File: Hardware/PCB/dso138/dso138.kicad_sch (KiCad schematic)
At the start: 41 parts, among them J1 Synth_power_2x5, J2 Conn_01x02, J3 Conn_01x02, J4 Conn_01x02, J5 Conn_02x04_Odd_Even, J6 Conn_02x04_Odd_Even, J7 Conn_02x04_Odd_Even, J8 Conn_02x04_Odd_Even, J9 Conn_01x02, SW1 SW_Push, SW2 SW_Push, SW3 SW_Push, SW4 SW_Push, SW5 SW_Push, SW6 SW_DP3T, SW7 SW_DP3T, SW8 SW_DP3T, U1 TL072, U2 L78L09_TO92

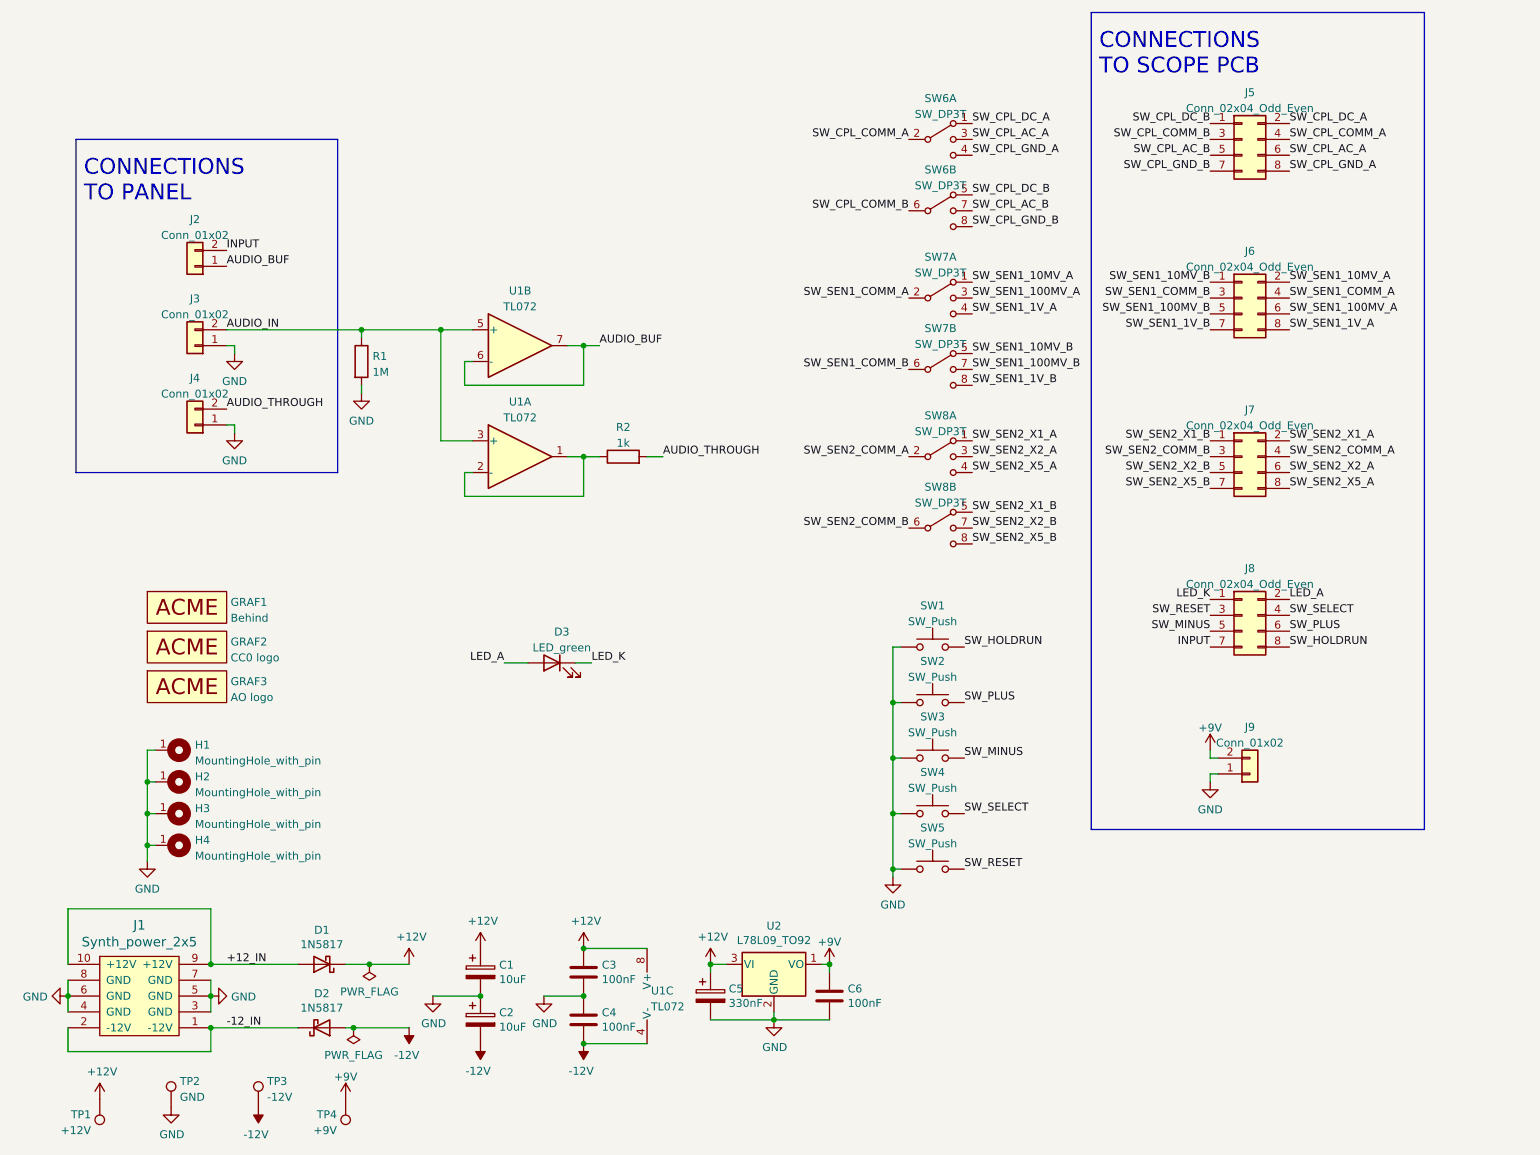
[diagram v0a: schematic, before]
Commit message: KiCad 7; Reorg schematic and add panel components & connectors; re-enable 3D models
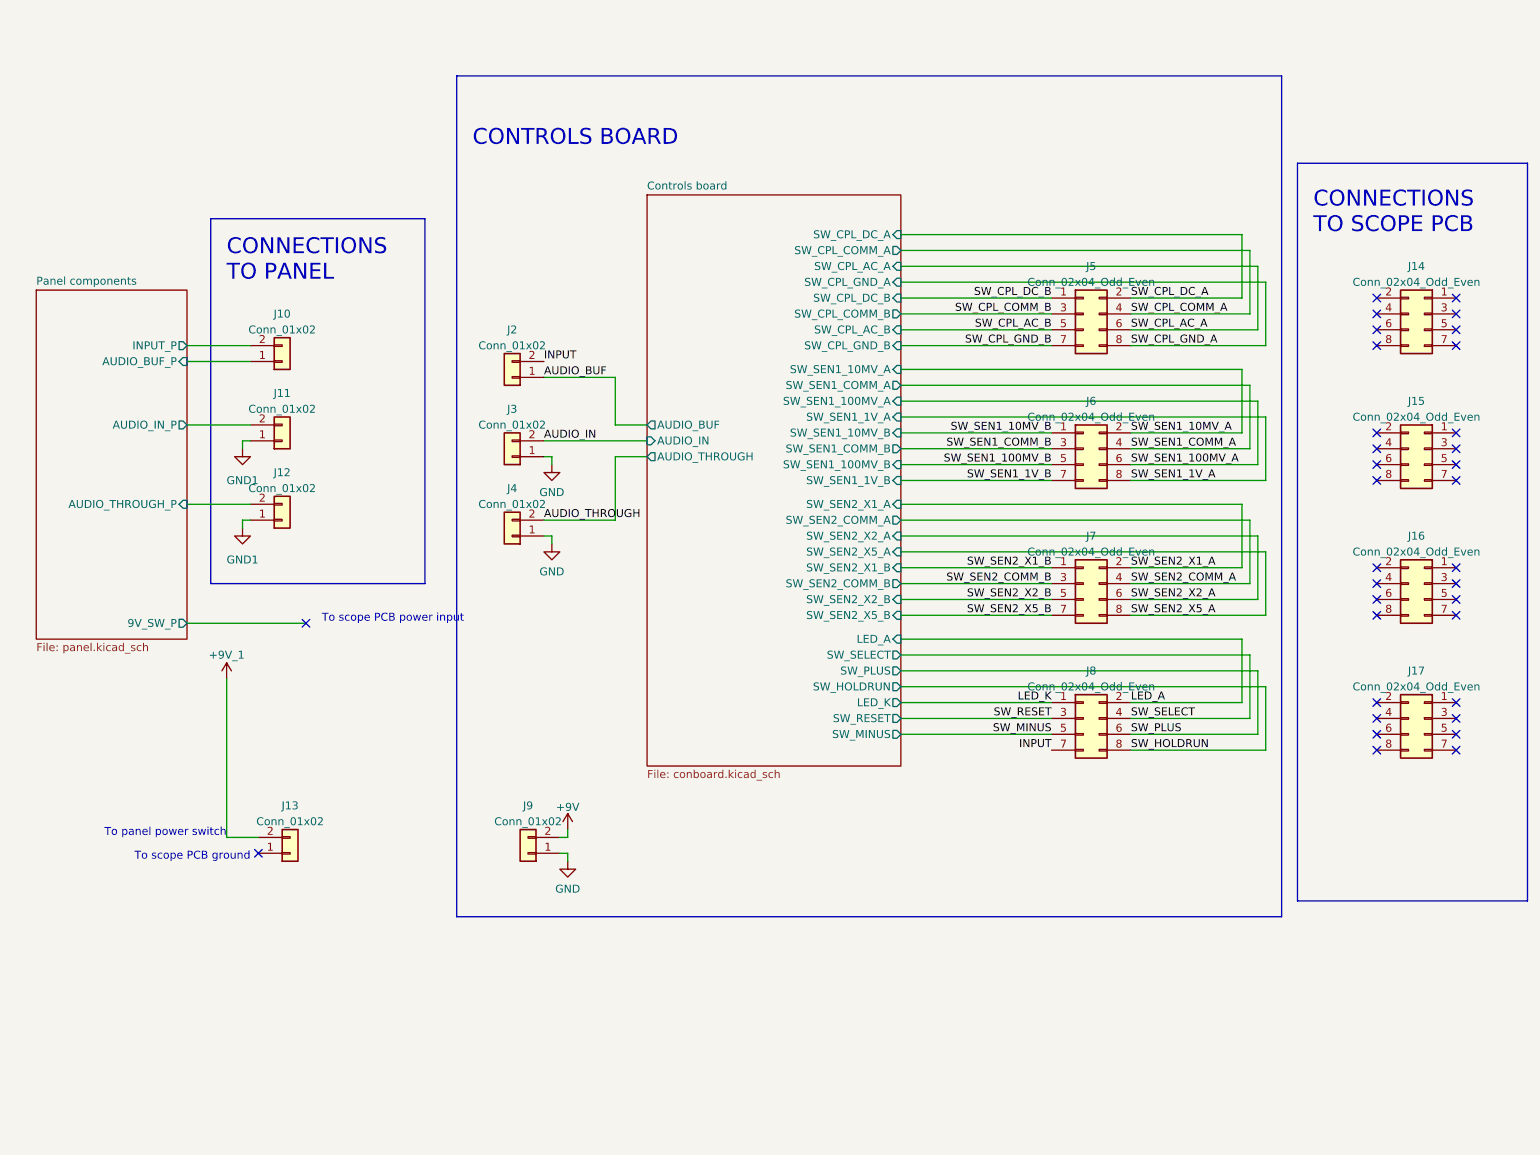
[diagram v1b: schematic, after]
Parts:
- removed C1, C2: 10uF, ao_tht:CP_Radial_D6.3mm_P2.50mm, symbol ao_symbols:CP
- removed C3, C4, C6: 100nF, ao_tht:C_Disc_D3.0mm_W1.6mm_P2.50mm, symbol ao_symbols:C
- removed C5: 330nF, ao_tht:CP_Radial_D6.3mm_P2.50mm, symbol ao_symbols:CP
- removed D1, D2: 1N5817, ao_tht:D_DO-41_SOD81_P10.16mm_Horizontal, symbol ao_symbols:1N5817
- removed D3: LED_green, ao_tht:LED_D5.0mm, symbol ao_symbols:LED_green
- removed GRAF1: Behind, dso138:dso138_behind, symbol ao_symbols:Graphic
- removed GRAF2: CC0 logo, ao_tht:CC0_logo, symbol ao_symbols:Graphic
- removed GRAF3: AO logo, ao_tht:analogoutput, symbol ao_symbols:Graphic
- removed H1, H2, H3, H4: MountingHole_with_pin, ao_tht:MountingHole_3.2mm_Pad, symbol ao_symbols:MountingHole_with_pin
- removed J1: Synth_power_2x5, ao_tht:Power_Header, symbol ao_symbols:Synth_power_2x5
- removed R1: 1M, ao_tht:R_Axial_DIN0207_L6.3mm_D2.5mm_P10.16mm_Horizontal, symbol ao_symbols:R
- removed R2: 1k, ao_tht:R_Axial_DIN0207_L6.3mm_D2.5mm_P10.16mm_Horizontal, symbol ao_symbols:R
- removed SW1, SW2, SW3, SW4, SW5: SW_Push, ao_tht:Tactile_E-switch_TL1100F160Q, symbol ao_symbols:SW_Push
- removed SW6, SW7, SW8: SW_DP3T, dso138:SW_CK_OS203012MU5QP1_DP3T, symbol dso138:SW_DP3T
- removed TP1: +12V, ao_tht:TestPoint_THTPad_D1.5mm_Drill0.7mm, symbol ao_symbols:TestPoint
- removed TP2: GND, ao_tht:TestPoint_THTPad_D1.5mm_Drill0.7mm, symbol ao_symbols:TestPoint
- removed TP3: -12V, ao_tht:TestPoint_THTPad_D1.5mm_Drill0.7mm, symbol ao_symbols:TestPoint
- removed TP4: +9V, ao_tht:TestPoint_THTPad_D1.5mm_Drill0.7mm, symbol ao_symbols:TestPoint
- removed U1: TL072, ao_tht:DIP-8_W7.62mm_Socket_LongPads, symbol ao_symbols:TL072
- removed U2: L78L09_TO92, ao_tht:TO-92_Inline_Wide, symbol ao_symbols:L78L09_TO92
- added J10, J11, J12, J13: Conn_01x02, Connector_JST:JST_XH_B2B-XH-A_1x02_P2.50mm_Vertical, symbol Connector_Generic:Conn_01x02
- added J14, J15, J16, J17: Conn_02x04_Odd_Even, Connector_IDC:IDC-Header_2x04_P2.54mm_Vertical, symbol Connector_Generic:Conn_02x04_Odd_Even
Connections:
- new net +9V_1: J13.2 (Pin_2)
- new net GND1: J11.1 (Pin_1), J12.1 (Pin_1)
- new net Panel components/AUDIO_BUF_P: J10.1 (Pin_1)
- new net Panel components/AUDIO_IN_P: J11.2 (Pin_2)
- new net Panel components/AUDIO_THROUGH_P: J12.2 (Pin_2)
- new net Panel components/INPUT_P: J10.2 (Pin_2)
- no-connect marks 0 -> 34
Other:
- added sheet Controls board (conboard.kicad_sch)
- added sheet Panel components (panel.kicad_sch)
- note added: "CONTROLS BOARD"
- note added: "To panel power switch"
- note added: "To scope PCB ground"
- note added: "To scope PCB power input"
- moved on the sheet: J2, J3, J4, J5, J6, J7, J8, J9

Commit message: Net classes, move 7809 and make horizontal, inverting buffers, power switch via PCB
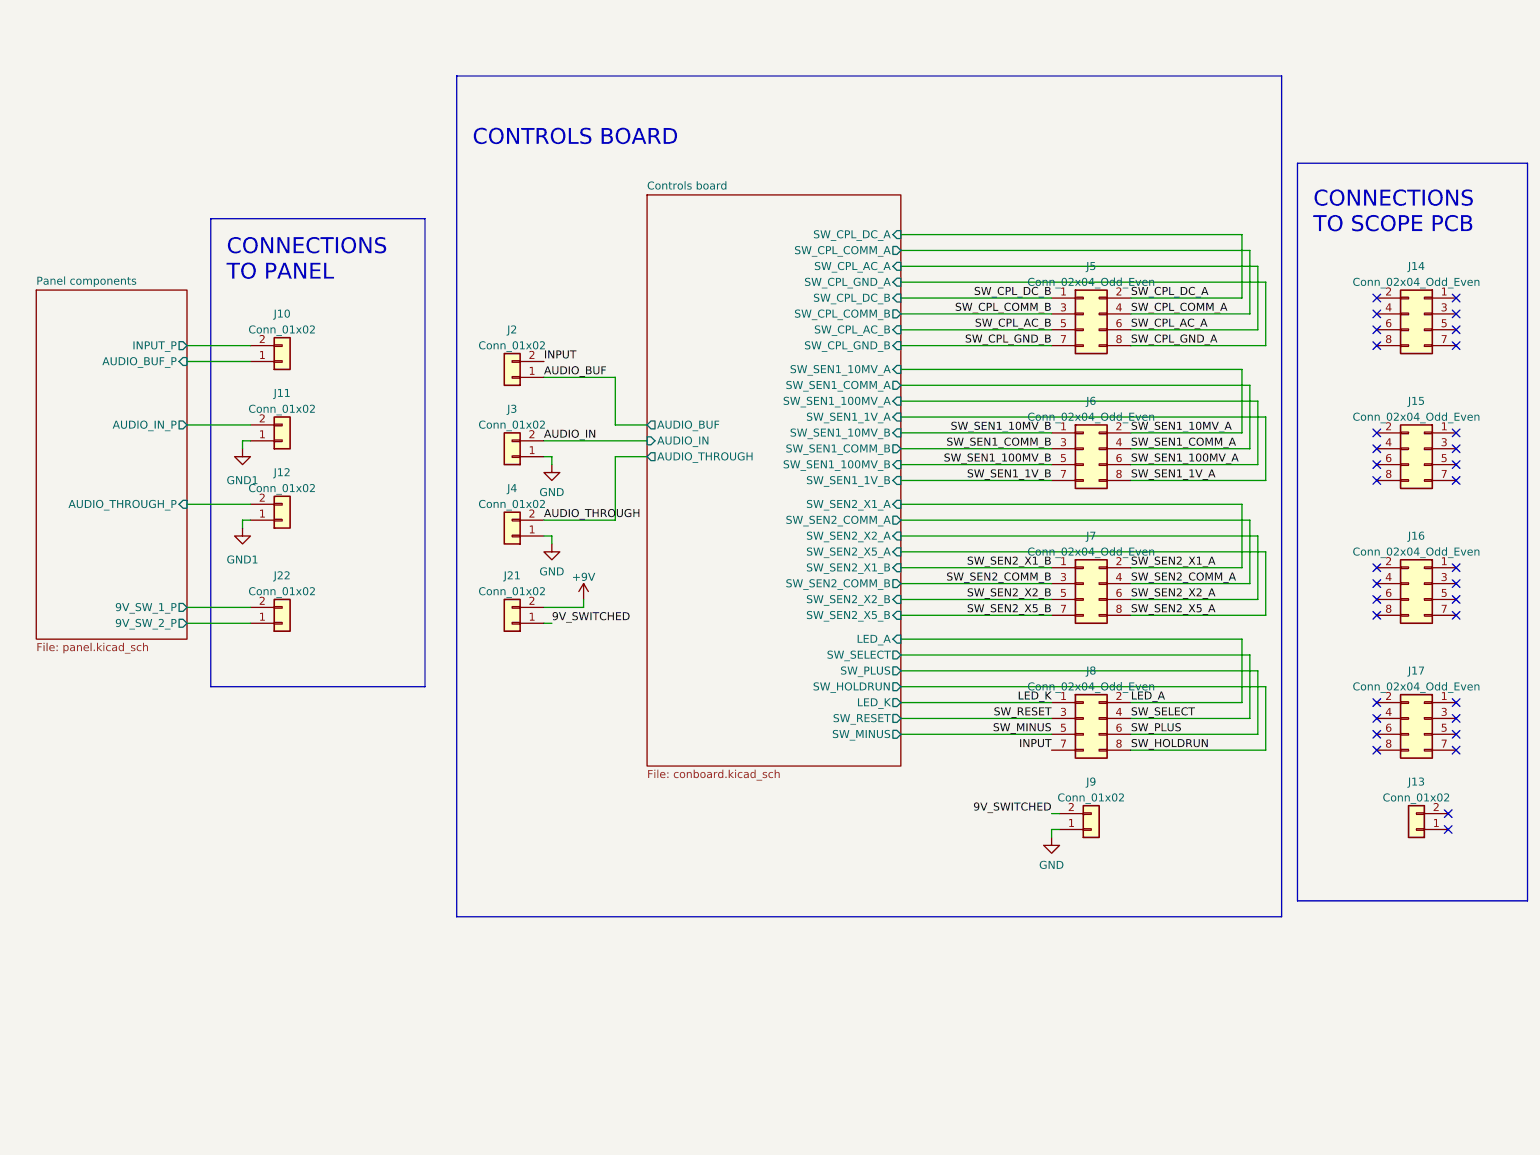
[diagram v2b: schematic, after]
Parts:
- added J21, J22: Conn_01x02, Connector_JST:JST_XH_B2B-XH-A_1x02_P2.50mm_Vertical, symbol Connector_Generic:Conn_01x02
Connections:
- net +9V: now also J21.2 (Pin_2); no longer J9.2 (Pin_2)
- net +9V_1: no longer names the net of J13.2 (Pin_2)
- new net 9V_SWITCHED: J21.1 (Pin_1), J9.2 (Pin_2)
- new net Panel components/9V_SW_1_P: J22.2 (Pin_2)
- new net Panel components/9V_SW_2_P: J22.1 (Pin_1)
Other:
- sheet Panel components ports: added 9V_SW_1_P, 9V_SW_2_P; removed 9V_SW_P
- note removed: "To panel power switch"
- note removed: "To scope PCB ground"
- note removed: "To scope PCB power input"
- moved on the sheet: J13, J9

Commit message: Mechanicals
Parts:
- added J1: DIP-8, symbol AO_symbols:DIP-8
- added W1, W2, W3, W4, W5: Ribbon_Cable, symbol AO_symbols:Ribbon_Cable
- added ZNU1, ZNU2, ZNU3, ZNU4, ZNU5, ZNU6, ZNU7, ZNU8, ZNU9: Nut, symbol AO_symbols:Nut
- added ZSC1, ZSC2, ZSC3, ZSC4, ZSC5, ZSC6, ZSC7, ZSC8, ZSC9: Screw, symbol AO_symbols:Screw
- added ZSP1, ZSP10, ZSP2, ZSP3, ZSP4, ZSP5, ZSP6, ZSP7, ZSP8, ZSP9: Spacer, symbol AO_symbols:Spacer
- J14: renamed from J9; Vendor (none) -> eBay
- J15: renamed from J13; footprint Connector_JST:JST_XH_B2B-XH-A_1x02_P2.50mm_Vertical -> (none); Vendor (none) -> eBay
- J2: renamed from J10; footprint Connector_JST:JST_XH_B2B-XH-A_1x02_P2.50mm_Vertical -> (none); Vendor (none) -> eBay
- J3: renamed from J11; footprint Connector_JST:JST_XH_B2B-XH-A_1x02_P2.50mm_Vertical -> (none); Vendor (none) -> eBay
- J4: renamed from J12; footprint Connector_JST:JST_XH_B2B-XH-A_1x02_P2.50mm_Vertical -> (none); Vendor (none) -> eBay
- J5: renamed from J22; footprint Connector_JST:JST_XH_B2B-XH-A_1x02_P2.50mm_Vertical -> (none); Vendor (none) -> eBay
- J6: renamed from J2; Vendor (none) -> eBay
- J7: renamed from J3; Vendor (none) -> eBay
- J8: renamed from J4; Vendor (none) -> eBay
- J9: renamed from J21; Vendor (none) -> eBay
- renumbered J5 to J10, J6 to J11, J7 to J12, J8 to J13, J14 to J16, J15 to J17, J16 to J18, J17 to J19
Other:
- note added: "HARDWARE"
- note added: "PANEL"
- note removed: "CONNECTIONS TO PANEL"
- moved on the sheet: J2, J3, J4, J5, J9

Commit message: STL file; BOM; documentation
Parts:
- added ZKN1, ZKN2, ZKN3, ZKN4, ZKN5: Switch cap, symbol AO_symbols:Knob
- added ZSC10, ZSC11: M2.5 screw 12 mm, symbol AO_symbols:Screw
- added ZSC12, ZSC13, ZSC14, ZSC15, ZSC16, ZSC17, ZSC18, ZSC19: Μ3 screw 6 mm, symbol AO_symbols:Screw
- added ZSP11, ZSP12: M3 spacer FF 10 mm, symbol AO_symbols:Spacer
- added ZSP13, ZSP14: M3 spacer FF 30 mm, symbol AO_symbols:Spacer
- J1: SKU (none) -> A-001; Vendor (none) -> Tayda
- J10, J11, J12, J13: SKU (none) -> A-2948; Vendor (none) -> Tayda
- J16, J17, J18, J19: SKU (none) -> A-3346; Vendor (none) -> Tayda
- W1, W2, W3, W4: value Ribbon_Cable -> 8 conductor ribbon cable ~ 20 cm
- W5: value Ribbon_Cable -> 40 conductor ribbon cable assembly with connectors (1 male, 1 female)
- ZNU1, ZNU2, ZNU3, ZNU4, ZNU5: value Nut -> M3 nut
- ZNU6, ZNU7, ZNU8, ZNU9: value Nut -> M2.5 nut
- ZSC1, ZSC2, ZSC3: value Screw -> Μ3 screw 6 mm
- ZSC4, ZSC5, ZSC6, ZSC7: value Screw -> Μ3 screw 12 mm
- ZSC8, ZSC9: value Screw -> M2.5 screw 12 mm
- ZSP1, ZSP2, ZSP3, ZSP4: value Spacer -> M3 spacer FF 5 mm
- ZSP10, ZSP9: value Spacer -> M3 spacer FF 10 mm
- ZSP5, ZSP6, ZSP7, ZSP8: value Spacer -> M2.5 spacer FF 5 mm
